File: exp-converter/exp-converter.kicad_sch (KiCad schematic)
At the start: 26 parts, among them J1 AudioJack2_Ground, J2 AudioJack2_Ground, J3 Conn_02x08_Odd_Even, J4 AudioJack2_Ground, J5 AudioJack2_Ground, U1 LM358, U2 LM358, U3 LM3046N, U4 LM358

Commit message: Exp. converter parts placed
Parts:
- added R10, R9: 100k, 00_exp-converter:R_Axial_DIN0207_L6.3mm_D2.5mm_P7.62mm_Horizontal, symbol Device:R
- added R7, R8: 1k, 00_exp-converter:R_Axial_DIN0207_L6.3mm_D2.5mm_P7.62mm_Horizontal, symbol Device:R
- added RV3, RV4: 10k, Potentiometer_THT:Potentiometer_Runtron_RM-065_Vertical, symbol Device:R_Potentiometer
- C3, C4: footprint Capacitor_THT:CP_Radial_D10.0mm_P2.50mm_P5.00mm -> Capacitor_THT:CP_Radial_D8.0mm_P2.50mm
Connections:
- net GND: now also U2.3 (+), U2.5 (+)
- net VCC: now also U4.8 (V+); no longer U4.4 (V-)
- net VEE: now also U4.4 (V-); no longer U4.8 (V+)
- net at RV2.3, U4.7: now also R8.1; no longer J5.T
- net at J1.T: now also R9.1; no longer U2.3 (+)
- net at C1.1, R1.2: now also U1.1; no longer U1.7
- net at C8.1, R5.2: now also U1.7; no longer U4.1
- net at J4.T: now also R10.1; no longer U2.5 (+)
- net at C1.2, R2.2, U3.1 (C): now also U1.2 (-); no longer U1.6 (-)
- net at U2.7, U3.6 (B): now also RV4.2, RV4.3; no longer U2.6 (-)
- net at C8.2, R4.2, U3.8 (C): now also U1.6 (-); no longer U4.2 (-)
- net at R3.1, U3.5 (C): now also U4.2 (-); no longer U1.2 (-)
- net at U2.1, U3.2 (B): now also RV3.2, RV3.3; no longer U2.2 (-)
- new net: R10.2, RV4.1, U2.6 (-)
- new net: R7.1, RV1.3, U4.1
- new net: R9.2, RV3.1, U2.2 (-)
- new net: J2.T, R7.2
- new net: J5.T, R8.2
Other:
- moved on the sheet: C1, C8, J1, J2, J4, J5, R1, R2, R3, R4, R5, R6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

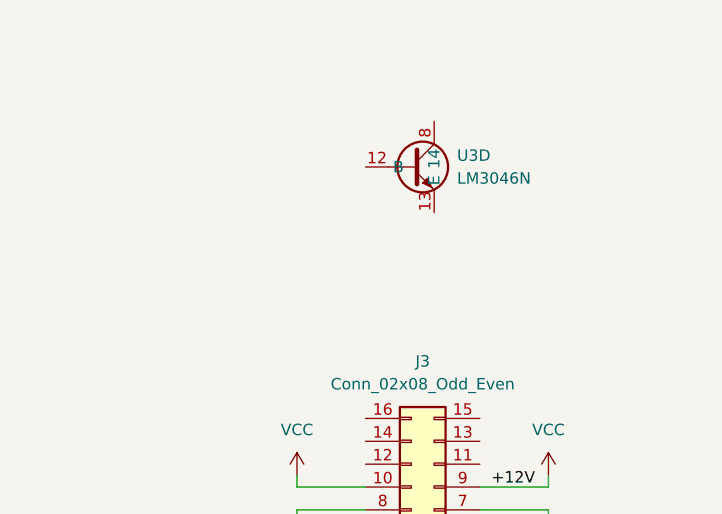
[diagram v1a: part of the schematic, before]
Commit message: Nearly finished exp converter PCB.
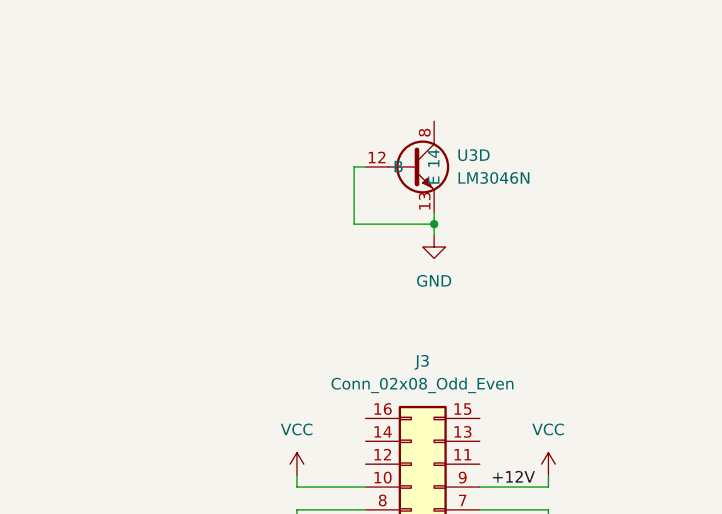
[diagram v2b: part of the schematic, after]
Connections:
- net GND: now also U3.12 (B), U3.13 (E)
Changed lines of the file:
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@@
 	)
 	(junction
+		(at 257.81 41.91)
+		(diameter 0)
+		(color 0 0 0 0)
+	)
+	(junction
 		(at 80.01 44.45)
 		(diameter 0)
@@
 	(wire
 		(pts
+			(xy 248.92 35.56) (xy 248.92 41.91)
+		)
+		(stroke
+			(width 0)
+			(type default)
+		)
+	)
+	(wire
+		(pts
 			(xy 146.05 22.86) (xy 140.97 22.86)
 		)
@@
 	(wire
 		(pts
+			(xy 250.19 35.56) (xy 248.92 35.56)
+		)
+		(stroke
+			(width 0)
+			(type default)
+		)
+	)
+	(wire
+		(pts
 			(xy 254 130.81) (xy 254 128.27)
 		)
@@
 	(wire
 		(pts
+			(xy 257.81 43.18) (xy 257.81 41.91)
+		)
+		(stroke
+			(width 0)
+			(type default)
+		)
+	)
+	(wire
+		(pts
 			(xy 36.83 41.91) (xy 50.8 41.91)
 		)
@@
 	(wire
 		(pts
+			(xy 257.81 41.91) (xy 257.81 40.64)
+		)
+		(stroke
+			(width 0)
+			(type default)
+		)
+	)
+	(wire
+		(pts
 			(xy 62.23 41.91) (xy 60.96 41.91)
 		)
@@
 		)
 	)
+	(wire
+		(pts
+			(xy 248.92 41.91) (xy 257.81 41.91)
+		)
+		(stroke
+			(width 0)
+			(type default)
+		)
+	)
 	(label "GND"
 		(at 270.51 80.01 0)
@@
 					(unit 1)
 				)
+			)
+		)
+	)
+	(symbol
+		(lib_id "power:GND")
+		(at 257.81 43.18 0)
+		(unit 1)
+		(exclude_from_sim no)
+		(in_bom yes)
+		(on_board yes)
+		(dnp no)
+		(fields_autoplaced yes)
+		(property "Reference" "#PWR024"
+			(at 257.81 49.53 0)
+			(effects
+				(font
+					(size 1.27 1.27)
+				)
+				(hide yes)
+			)
+		)
+		(property "Value" "GND"
+			(at 257.81 48.26 0)
+			(effects
+				(font
+					(size 1.27 1.27)
+				)
+			)
+		)
+		(property "Footprint" ""
+			(at 257.81 43.18 0)
+			(effects
+				(font
+					(size 1.27 1.27)
+				)
+				(hide yes)
+			)
+		)
+		(property "Datasheet" ""
+			(at 257.81 43.18 0)
+			(effects
+				(font
+					(size 1.27 1.27)
+				)
+				(hide yes)
+			)
+		)
+		(property "Description" "Power symbol creates a global label with name \"GND\" , ground"
+			(at 257.81 43.18 0)
+			(effects
+				(font
+					(size 1.27 1.27)
+				)
+				(hide yes)
+			)
+		)
+		(pin "1"
+		)
+		(instances
+			(project "exp-converter"
+				(path "/e04193b9-64b6-43c3-8e95-9a6a215f7105"
+					(reference "#PWR024")
+					(unit 1)
+				)
